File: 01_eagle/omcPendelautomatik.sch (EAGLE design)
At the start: 70 parts, among them IC1 PIC12F675, IC2 7805, IC3 L5970D, K1 NA-5V, T1 BSS138, T2 BSS138, X1 RT034 Typ 086, X2 PH2X3

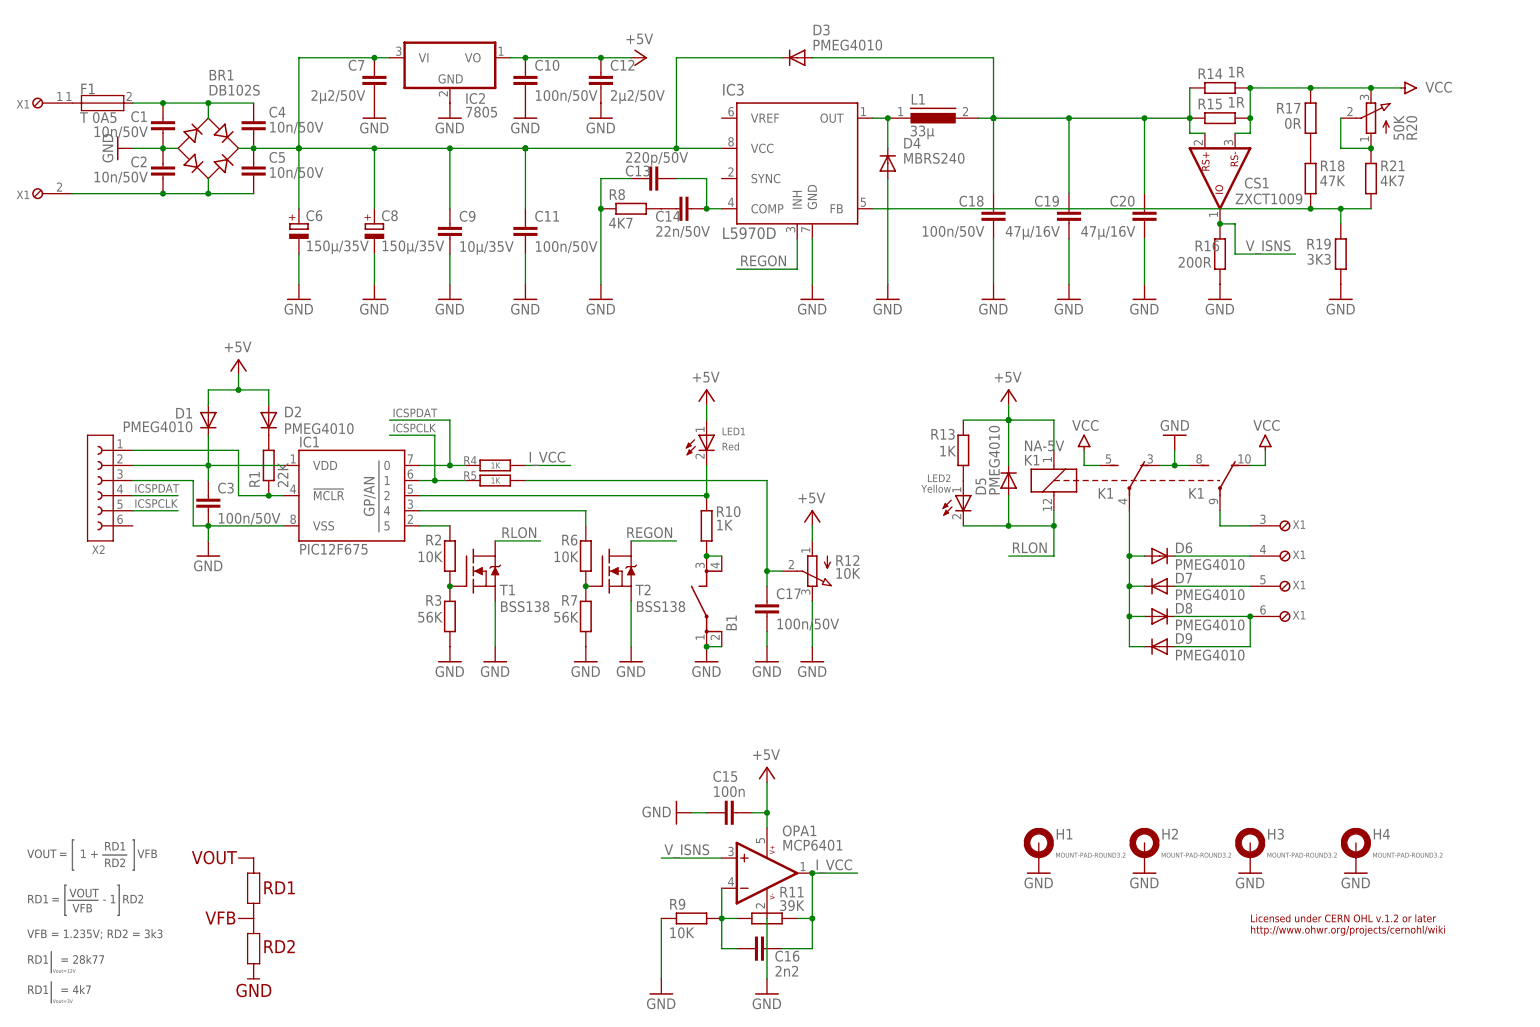
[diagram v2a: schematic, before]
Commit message: omcPendelautomatik -> Placement and routing main parts done -> schematic changes for routing
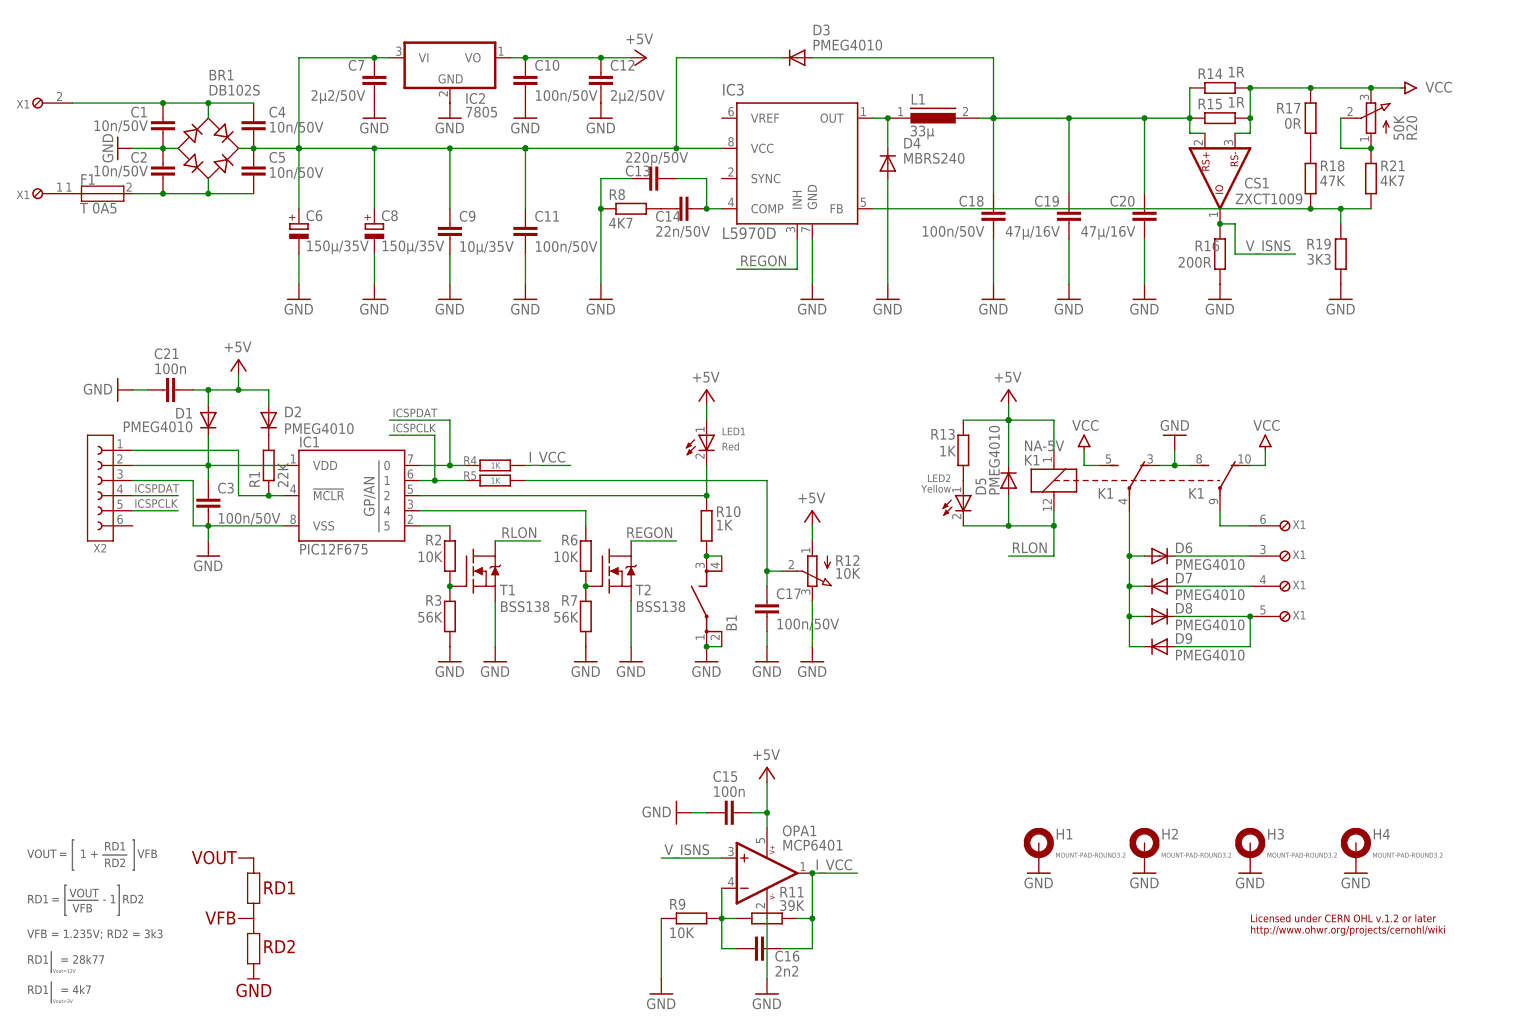
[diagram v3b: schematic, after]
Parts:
- added C21: 100n, omcCapacitor:X7R-100000P-1206
- X2: value PH2X3 -> 2X3; device omcConnector:PH2X3-SMD1.27 -> omcConnector:BOXHD-06-S-2.54
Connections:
- removed net N$25: D8.C, D9.A, X1G$6.P$1
- new net N$29: D8.C, D9.A, X1G$5.P$1
- net +5V: now also C21.2
- net GND: now also C21.1, X23.P$1; no longer X2G$3.P$1
- net ICSPCLK: now also X25.P$1; no longer X2G$5.P$1
- net ICSPDAT: now also X24.P$1; no longer X2G$4.P$1
- net N$10: now also X21.P$1; no longer X2G$1.P$1
- net N$17: now also X1G$2.P$1; no longer F1.P$2
- net N$18: now also X1G$3.P$1; no longer X1G$4.P$1
- net N$21: now also X1G$4.P$1; no longer X1G$5.P$1
- net N$23: now also F1.P$2; no longer X1G$2.P$1
- net N$24: now also X1G$6.P$1; no longer X1G$3.P$1
- net N$7: now also X22.P$1; no longer X2G$2.P$1
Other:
- moved on the sheet: F1, X1
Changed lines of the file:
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@@
 <setting verticaltext="up"/>
 </settings>
-<grid distance="0.1" unitdist="inch" unit="inch" style="lines" multiple="1" display="yes" altdistance="0.01" altunitdist="inch" altunit="inch"/>
+<grid distance="0.1" unitdist="inch" unit="inch" style="lines" multiple="1" display="no" altdistance="0.01" altunitdist="inch" altunit="inch"/>
 <layers>
 <layer number="1" name="Top" color="4" fill="1" visible="no" active="no"/>
@@
 <part name="C15" library="omcCapacitor" deviceset="X7R" device="-1206" technology="-100000P" value="100n"/>
 <part name="GND17" library="supply1" deviceset="GND" device=""/>
-<part name="X2" library="omcConnector" deviceset="PH2X3" device="-SMD1.27" value="PH2X3"/>
+<part name="X2" library="omcConnector" deviceset="BOXHD-06" device="-2.54" technology="-S" value="2X3"/>
+<part name="C21" library="omcCapacitor" deviceset="X7R" device="-1206" technology="-100000P" value="100n"/>
+<part name="GND34" library="supply1" deviceset="GND" device=""/>
 </parts>
 <sheets>
@@
 </instance>
 <instance part="GND29" gate="1" x="203.2" y="104.14" rot="R180"/>
-<instance part="X1" gate="G$1" x="12.7" y="160.02"/>
-<instance part="X1" gate="G$2" x="12.7" y="144.78"/>
-<instance part="X1" gate="G$3" x="220.98" y="88.9" rot="R180"/>
-<instance part="X1" gate="G$4" x="220.98" y="83.82" rot="R180"/>
-<instance part="X1" gate="G$5" x="220.98" y="78.74" rot="R180"/>
-<instance part="X1" gate="G$6" x="220.98" y="73.66" rot="R180"/>
+<instance part="X1" gate="G$1" x="12.7" y="144.78"/>
+<instance part="X1" gate="G$2" x="12.7" y="160.02"/>
+<instance part="X1" gate="G$3" x="220.98" y="83.82" rot="R180"/>
+<instance part="X1" gate="G$4" x="220.98" y="78.74" rot="R180"/>
+<instance part="X1" gate="G$5" x="220.98" y="73.66" rot="R180"/>
+<instance part="X1" gate="G$6" x="220.98" y="88.9" rot="R180"/>
 <instance part="BR1" gate="G$1" x="40.64" y="152.4" smashed="yes">
 <attribute name="VALUE" x="40.64" y="161.29" size="1.778" layer="96"/>
@@
 <instance part="C8" gate="G$1" x="68.58" y="139.7"/>
 <instance part="C1" gate="G$1" x="33.02" y="157.48" smashed="yes">
-<attribute name="NAME" x="30.48" y="158.623" size="1.778" layer="95" rot="R180"/>
-<attribute name="VALUE" x="30.48" y="156.083" size="1.778" layer="96" rot="R180"/>
+<attribute name="NAME" x="30.48" y="159.385" size="1.778" layer="95" rot="R180"/>
+<attribute name="VALUE" x="30.48" y="157.099" size="1.778" layer="96" rot="R180"/>
 </instance>
 <instance part="C2" gate="G$1" x="33.02" y="149.86" smashed="yes">
-<attribute name="NAME" x="30.48" y="151.003" size="1.778" layer="95" rot="R180"/>
-<attribute name="VALUE" x="30.48" y="148.463" size="1.778" layer="96" rot="R180"/>
+<attribute name="NAME" x="30.48" y="151.765" size="1.778" layer="95" rot="R180"/>
+<attribute name="VALUE" x="30.48" y="149.479" size="1.778" layer="96" rot="R180"/>
 </instance>
 <instance part="GND1" gate="1" x="25.4" y="152.4" rot="R270"/>
@@
 <instance part="GND5" gate="1" x="68.58" y="127"/>
 <instance part="GND3" gate="1" x="55.88" y="127"/>
-<instance part="F1" gate="G$1" x="22.86" y="160.02"/>
+<instance part="F1" gate="G$1" x="22.86" y="144.78"/>
 <instance part="D6" gate="G$1" x="200.66" y="83.82"/>
 <instance part="D9" gate="G$1" x="200.66" y="68.58" smashed="yes" rot="R180">
@@
 <attribute name="VALUE" x="113.538" y="39.878" size="1.778" layer="96"/>
 </instance>
-<instance part="X2" gate="G$1" x="22.86" y="101.6" smashed="yes" rot="R180"/>
-<instance part="X2" gate="G$2" x="22.86" y="99.06" smashed="yes"/>
-<instance part="X2" gate="G$3" x="22.86" y="96.52" smashed="yes" rot="R180"/>
-<instance part="X2" gate="G$4" x="22.86" y="93.98" smashed="yes"/>
-<instance part="X2" gate="G$5" x="22.86" y="91.44" smashed="yes" rot="R180"/>
-<instance part="X2" gate="G$6" x="22.86" y="88.9" smashed="yes">
-<attribute name="PART" x="23.368" y="85.598" size="1.4224" layer="95" rot="R180"/>
+<instance part="X2" gate="1" x="22.86" y="101.6" smashed="yes" rot="R180"/>
+<instance part="X2" gate="3" x="22.86" y="96.52" smashed="yes" rot="R180"/>
+<instance part="X2" gate="5" x="22.86" y="91.44" smashed="yes" rot="R180"/>
+<instance part="X2" gate="2" x="22.86" y="99.06" smashed="yes"/>
+<instance part="X2" gate="4" x="22.86" y="93.98" smashed="yes"/>
+<instance part="X2" gate="6" x="22.86" y="88.9" smashed="yes">
+<attribute name="PART" x="23.622" y="85.852" size="1.4224" layer="95" rot="R180"/>
+</instance>
+<instance part="C21" gate="G$1" x="33.02" y="111.76" smashed="yes" rot="R90">
+<attribute name="NAME" x="31.496" y="116.967" size="1.778" layer="95"/>
+<attribute name="VALUE" x="31.496" y="114.427" size="1.778" layer="96"/>
+</instance>
+<instance part="GND34" gate="1" x="25.4" y="111.76" smashed="yes" rot="R270">
+<attribute name="VALUE" x="19.558" y="110.998" size="1.778" layer="96"/>
 </instance>
 </instances>
@@
 <wire x1="38.1" y1="88.9" x2="40.64" y2="88.9" width="0.1524" layer="91"/>
 <pinref part="IC1" gate="G$1" pin="VSS"/>
-<pinref part="X2" gate="G$3" pin="P$1"/>
+<pinref part="X2" gate="3" pin="P$1"/>
 </segment>
 <segment>
@@
 <pinref part="GND17" gate="1" pin="GND"/>
 <wire x1="124.46" y1="40.64" x2="121.92" y2="40.64" width="0.1524" layer="91"/>
+</segment>
+<segment>
+<pinref part="C21" gate="G$1" pin="1"/>
+<pinref part="GND34" gate="1" pin="GND"/>
+<wire x1="30.48" y1="111.76" x2="27.94" y2="111.76" width="0.1524" layer="91"/>
 </segment>
 </net>
@@
 <pinref part="D1" gate="G$1" pin="A"/>
 <pinref part="D2" gate="G$1" pin="A"/>
+<pinref part="C21" gate="G$1" pin="2"/>
+<wire x1="38.1" y1="111.76" x2="40.64" y2="111.76" width="0.1524" layer="91"/>
+<junction x="40.64" y="111.76"/>
 </segment>
 <segment>
@@
 <wire x1="33.02" y1="144.78" x2="40.64" y2="144.78" width="0.1524" layer="91"/>
 <wire x1="40.64" y1="144.78" x2="40.64" y2="147.32" width="0.1524" layer="91"/>
-<pinref part="X1" gate="G$2" pin="P$1"/>
-<wire x1="17.78" y1="144.78" x2="33.02" y2="144.78" width="0.1524" layer="91"/>
-<junction x="33.02" y="144.78"/>
 <pinref part="C5" gate="G$1" pin="2"/>
 <wire x1="40.64" y1="144.78" x2="48.26" y2="144.78" width="0.1524" layer="91"/>
 <junction x="40.64" y="144.78"/>
+<pinref part="F1" gate="G$1" pin="P$2"/>
+<wire x1="27.94" y1="144.78" x2="33.02" y2="144.78" width="0.1524" layer="91"/>
+<junction x="33.02" y="144.78"/>
 </segment>
 </net>
@@
 <wire x1="40.64" y1="160.02" x2="48.26" y2="160.02" width="0.1524" layer="91"/>
 <junction x="40.64" y="160.02"/>
-<pinref part="F1" gate="G$1" pin="P$2"/>
-<wire x1="27.94" y1="160.02" x2="33.02" y2="160.02" width="0.1524" layer="91"/>
+<wire x1="17.78" y1="160.02" x2="33.02" y2="160.02" width="0.1524" layer="91"/>
 <junction x="33.02" y="160.02"/>
+<pinref part="X1" gate="G$2" pin="P$1"/>
 </segment>
 </net>
@@
 <net name="N$24" class="0">
 <segment>
-<pinref part="X1" gate="G$3" pin="P$1"/>
-<wire x1="215.9" y1="88.9" x2="210.82" y2="88.9" width="0.1524" layer="91"/>
 <pinref part="K1" gate="G$2" pin="P"/>
 <wire x1="210.82" y1="88.9" x2="210.82" y2="91.44" width="0.1524" layer="91"/>
-</segment>
-</net>
-<net name="N$18" class="0">
-<segment>
-<pinref part="D6" gate="G$1" pin="C"/>
-<pinref part="X1" gate="G$4" pin="P$1"/>
-<wire x1="203.2" y1="83.82" x2="215.9" y2="83.82" width="0.1524" layer="91"/>
-</segment>
-</net>
-<net name="N$21" class="0">
-<segment>
-<pinref part="D7" gate="G$1" pin="A"/>
-<pinref part="X1" gate="G$5" pin="P$1"/>
-<wire x1="203.2" y1="78.74" x2="215.9" y2="78.74" width="0.1524" layer="91"/>
-</segment>
-</net>
-<net name="N$25" class="0">
-<segment>
-<pinref part="D9" gate="G$1" pin="A"/>
-<wire x1="203.2" y1="68.58" x2="215.9" y2="68.58" width="0.1524" layer="91"/>
 <pinref part="X1" gate="G$6" pin="P$1"/>
-<wire x1="215.9" y1="68.58" x2="215.9" y2="73.66" width="0.1524" layer="91"/>
-<pinref part="D8" gate="G$1" pin="C"/>
-<wire x1="203.2" y1="73.66" x2="215.9" y2="73.66" width="0.1524" layer="91"/>
-<junction x="215.9" y="73.66"/>
+<wire x1="210.82" y1="88.9" x2="215.9" y2="88.9" width="0.1524" layer="91"/>
 </segment>
 </net>
@@
 <pinref part="IC1" gate="G$1" pin="VDD"/>
 <pinref part="D1" gate="G$1" pin="C"/>
-<pinref part="X2" gate="G$2" pin="P$1"/>
+<pinref part="X2" gate="2" pin="P$1"/>
 </segment>
 </net>
@@
 <wire x1="45.72" y1="101.6" x2="27.94" y2="101.6" width="0.1524" layer="91"/>
 <pinref part="IC1" gate="G$1" pin="!MCLR!"/>
-<pinref part="X2" gate="G$1" pin="P$1"/>
+<pinref part="X2" gate="1" pin="P$1"/>
 </segment>
 </net>
@@
 <wire x1="27.94" y1="93.98" x2="35.56" y2="93.98" width="0.1524" layer="91"/>
 <label x="28.194" y="94.488" size="1.4224" layer="95"/>
-<pinref part="X2" gate="G$4" pin="P$1"/>
+<pinref part="X2" gate="4" pin="P$1"/>
 </segment>
 <segment>
@@
 <wire x1="27.94" y1="91.44" x2="35.56" y2="91.44" width="0.1524" layer="91"/>
 <label x="28.194" y="91.948" size="1.4224" layer="95"/>
-<pinref part="X2" gate="G$5" pin="P$1"/>
+<pinref part="X2" gate="5" pin="P$1"/>
 </segment>
 <segment>
@@
 </segment>
 </net>
+<net name="N$18" class="0">
+<segment>
+<pinref part="D6" gate="G$1" pin="C"/>
+<pinref part="X1" gate="G$3" pin="P$1"/>
+<wire x1="203.2" y1="83.82" x2="215.9" y2="83.82" width="0.1524" layer="91"/>
+</segment>
+</net>
+<net name="N$21" class="0">
+<segment>
+<pinref part="D7" gate="G$1" pin="A"/>
+<pinref part="X1" gate="G$4" pin="P$1"/>
+<wire x1="203.2" y1="78.74" x2="215.9" y2="78.74" width="0.1524" layer="91"/>
+</segment>
+</net>
+<net name="N$29" class="0">
+<segment>
+<pinref part="D9" gate="G$1" pin="A"/>
+<wire x1="203.2" y1="68.58" x2="215.9" y2="68.58" width="0.1524" layer="91"/>
+<pinref part="D8" gate="G$1" pin="C"/>
+<pinref part="X1" gate="G$5" pin="P$1"/>
+<wire x1="203.2" y1="73.66" x2="215.9" y2="73.66" width="0.1524" layer="91"/>
+<wire x1="215.9" y1="68.58" x2="215.9" y2="73.66" width="0.1524" layer="91"/>
+<junction x="215.9" y="73.66"/>
+</segment>
+</net>

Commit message: omcPendelautomatik -> symbol update -> added some vias to connect top/bottom ground plane
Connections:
- net GND: now also IC2.GND@1; no longer IC2.GND
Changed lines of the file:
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@@
 <segment>
 <pinref part="GND6" gate="1" pin="GND"/>
-<pinref part="IC2" gate="G$1" pin="GND"/>
+<pinref part="IC2" gate="G$1" pin="GND@1"/>
 </segment>
 <segment>
